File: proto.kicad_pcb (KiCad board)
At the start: 2 copper layers, 128 x 50.1 mm, 54 parts, among them IC1 WM8960CGEFL_V, J1 Micro_SD_Card, J10 CS, J11 BL, J12 BAT+, J13 BAT-, J14 L-, J15 L+, J16 R-, J17 R+, J2 AudioJack3, J3 USB_C_Receptacle_PowerOnly_6P, J4 GND, J5 VCC, J6 SCL, J7 SDA, J8 RES, J9 DC, SW1 SW_Push, SW2 SW_Push, SW3 SW_Push, SW4 SW_Push, SW5 SW_Push, SW6 SW_Push, SW7 SW_Push, SW8 SW_Push, U2 BQ24074RGT

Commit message: Fix PCB speaker markings
(R+ R- to L+ L-)
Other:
- board text added: "L+"
- board text added: "L-"

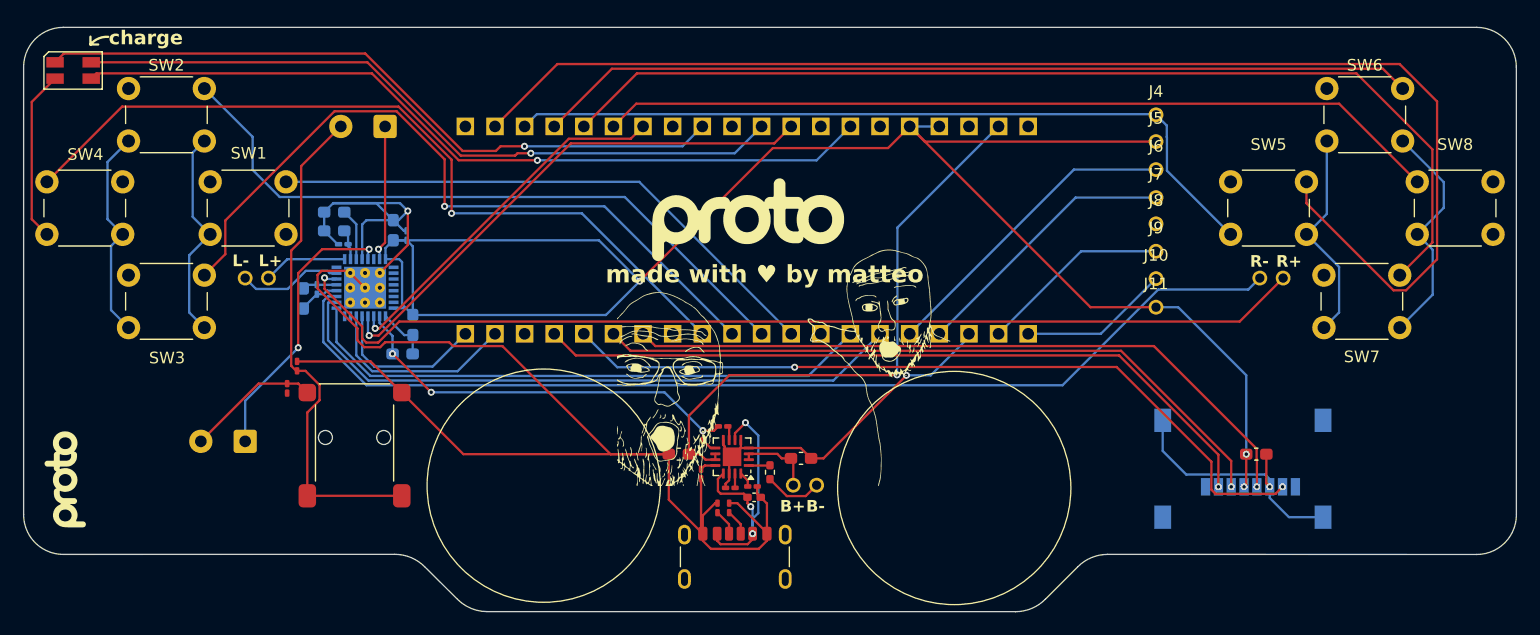
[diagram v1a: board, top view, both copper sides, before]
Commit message: Update hardware & software
Added a voltage divider to be able to measure battery level and added very basic firmware
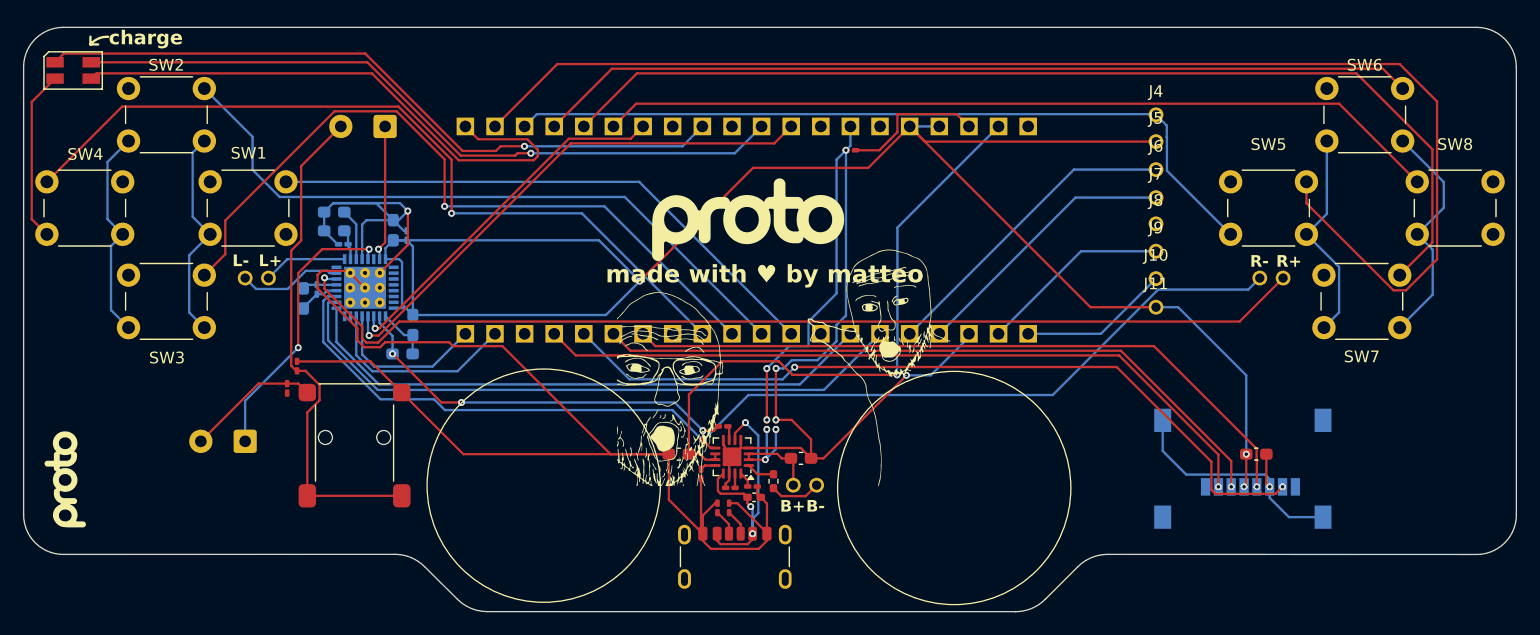
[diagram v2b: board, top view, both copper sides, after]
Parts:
- added C16: 100nF, Capacitor_SMD:C_0201_0603Metric_Pad0.64x0.40mm_HandSolder, F.Cu at (178.9, 96.0)
- added R10: 1M, Resistor_SMD:R_0201_0603Metric_Pad0.64x0.40mm_HandSolder, F.Cu at (172.5, 119.6)
- added R11: 1M, Resistor_SMD:R_0201_0603Metric_Pad0.64x0.40mm_HandSolder, F.Cu at (171.7, 119.6)
- moved TH1 0.83 mm to (172.3, 124.4)
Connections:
- C1 pad 2: GND -> BAT+
- C10 pad 1: GND -> BAT+
- C11 pad 1: GND -> BAT+
- C12 pad 1: GND -> BAT+
- C13 pad 1: GND -> BAT+
- C14 pad 1: GND -> BAT+
- C15 pad 1: GND -> BAT+
- C2 pad 2: GND -> BAT+
- C3 pad 2: GND -> BAT+
- C6 pad 2: GND -> BAT+
- C7 pad 2: GND -> BAT+
- C8 pad 2: GND -> BAT+
- C9 pad 2: GND -> BAT+
- D1 pad 4: GND -> BAT+
- IC1 pad 20: GND -> BAT+
- IC1 pad 24: GND -> BAT+
- IC1 pad 28: GND -> BAT+
- IC1 pad 33: GND -> BAT+
- IC1 pad 9: GND -> BAT+
- IC1 pad P$1: GND -> BAT+
- IC1 pad P$2: GND -> BAT+
- IC1 pad P$3: GND -> BAT+
- IC1 pad P$4: GND -> BAT+
- IC1 pad P$5: GND -> BAT+
- IC1 pad P$6: GND -> BAT+
- IC1 pad P$7: GND -> BAT+
- IC1 pad P$8: GND -> BAT+
- IC1 pad P$9: GND -> BAT+
- J1 pad 6: GND -> BAT+
- J1 pad SH: GND -> BAT+
- J2 pad S: GND -> BAT+
- J3 pad A12: GND -> BAT+
- J3 pad B12: GND -> BAT+
- J3 pad SH: GND -> BAT+
- J4 pad 1: GND -> BAT+
- R1 pad 1: GND -> BAT+
- R2 pad 1: GND -> BAT+
- R3 pad 2: GND -> BAT+
- R4 pad 2: GND -> BAT+
- R5 pad 2: GND -> BAT+
- R8 pad 1: GND -> BAT+
- R9 pad 1: GND -> BAT+
- SW1 pad 2: GND -> BAT+
- SW2 pad 2: GND -> BAT+
- SW3 pad 2: GND -> BAT+
- SW4 pad 2: GND -> BAT+
- SW5 pad 2: GND -> BAT+
- SW6 pad 2: GND -> BAT+
- SW7 pad 2: GND -> BAT+
- SW8 pad 2: GND -> BAT+
- U1 pad 3V3: +3.3V -> (no net)
- U1 pad GND: (no net) -> BAT+
- U1 pad GP0: CS -> (no net)
- U1 pad GP1: DC -> (no net)
- U1 pad GP22: B -> (no net)
- U1 pad GP26_A0: R -> (no net)
- U1 pad GP28_A2: G -> BAT+
- U2 pad 14: GND -> BAT+
- U2 pad 17: GND -> BAT+
- U2 pad 4: GND -> BAT+
- U2 pad 5: GND -> BAT+
- U2 pad 8: GND -> BAT+
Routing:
- net BAT+: track 6.66 -> 449.5 mm, vias 0 -> 11
- net GND: track 361.7 -> 0.00 mm, vias 3 -> 0
- net G: track 69.6 -> 49.3 mm, vias 1 -> 0
- net Net-(IC1-SPK_RN): track 90.4 -> 94.2 mm
- net VSYS: track 50.5 -> 52.5 mm
- net MISO: track 67.3 -> 68.1 mm
- net SDIN: track 54.4 -> 55.0 mm
- net BAT-: track 4.99 -> 4.37 mm
- net SCLK: track 49.7 -> 50.3 mm
- net TS: track 1.85 -> 2.43 mm

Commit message: UPDATED stuff again for software + hello world
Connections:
- U1 pad GP14: (no net) -> BLCK
- U1 pad GP27_A1: (no net) -> DACDAT
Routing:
- net DACDAT: track 17.1 -> 51.5 mm, vias 0 -> 1
- net BLCK: track 45.3 -> 14.9 mm, vias 1 -> 2
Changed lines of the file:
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@@
 			(layers "*.Cu" "*.Mask")
 			(remove_unused_layers no)
+			(net "BLCK")
 			(solder_mask_margin 0.102)
 		)
@@
 			(layers "*.Cu" "*.Mask")
 			(remove_unused_layers no)
+			(net "DACDAT")
 			(solder_mask_margin 0.102)
 		)
@@
 	)
 	(segment
-		(start 157.9325 110.1675)
-		(end 141.38 110.1675)
-		(width 0.2)
-		(layer "B.Cu")
-		(net "+3.3V")
-	)
-	(segment
 		(start 139.7025 103.76)
 		(end 157.33147 103.76)
@@
 	)
 	(segment
+		(start 158.574 109.526)
+		(end 142.0215 109.526)
+		(width 0.2)
+		(layer "B.Cu")
+		(net "+3.3V")
+	)
+	(segment
 		(start 207 109.5)
 		(end 205.1 109.5)
@@
 	)
 	(segment
-		(start 212.8375 115.3375)
-		(end 207 109.5)
+		(start 142.0215 109.526)
+		(end 141.38 110.1675)
 		(width 0.2)
 		(layer "B.Cu")
@@
 	)
 	(segment
-		(start 160.835735 107.264265)
-		(end 157.9325 110.1675)
+		(start 212.8375 115.3375)
+		(end 207 109.5)
 		(width 0.2)
 		(layer "B.Cu")
@@
 	)
 	(segment
+		(start 160.835735 107.264265)
+		(end 158.574 109.526)
+		(width 0.2)
+		(layer "B.Cu")
+		(net "+3.3V")
+	)
+	(segment
 		(start 157.33147 103.76)
 		(end 160.835735 107.264265)
@@
 	)
 	(segment
-		(start 154.920346 95.454)
-		(end 172.366 95.454)
+		(start 138.443849 111.930497)
+		(end 137.63 111.930497)
 		(width 0.2)
 		(layer "F.Cu")
@@
 	)
 	(segment
-		(start 172.366 95.454)
-		(end 173.82 94)
+		(start 140.248346 110.126)
+		(end 138.443849 111.930497)
 		(width 0.2)
 		(layer "F.Cu")
@@
 	)
 	(segment
-		(start 138.443849 111.930497)
-		(end 154.920346 95.454)
+		(start 148.42 110.126)
+		(end 140.248346 110.126)
 		(width 0.2)
 		(layer "F.Cu")
 		(net "BLCK")
 	)
-	(segment
-		(start 137.63 111.930497)
-		(end 138.443849 111.930497)
-		(width 0.2)
-		(layer "F.Cu")
+	(via
+		(at 148.42 110.126)
+		(size 0.6)
+		(drill 0.3)
+		(layers "F.Cu" "B.Cu")
 		(net "BLCK")
 	)
@@
 	)
 	(segment
+		(start 148.42 110.126)
+		(end 148.42 111.78)
+		(width 0.2)
+		(layer "B.Cu")
+		(net "BLCK")
+	)
+	(segment
 		(start 137.53 111.88)
 		(end 137.53 110.28)
@@
 	)
 	(segment
-		(start 137.897592 114.99)
-		(end 145.21 114.99)
+		(start 149.91 110.126)
+		(end 157.108 110.126)
+		(width 0.2)
+		(layer "F.Cu")
+		(net "DACDAT")
+	)
+	(segment
+		(start 173.234 94)
+		(end 173.82 94)
+		(width 0.2)
+		(layer "F.Cu")
+		(net "DACDAT")
+	)
+	(segment
+		(start 157.108 110.126)
+		(end 173.234 94)
+		(width 0.2)
+		(layer "F.Cu")
+		(net "DACDAT")
+	)
+	(via
+		(at 149.91 110.126)
+		(size 0.6)
+		(drill 0.3)
+		(layers "F.Cu" "B.Cu")
+		(net "DACDAT")
+	)
+	(segment
+		(start 149.91 110.126)
+		(end 149.91 110.722)
 		(width 0.2)
 		(layer "B.Cu")
@@
 	)
 	(segment
-		(start 145.21 114.99)
-		(end 148.42 111.78)
+		(start 149.906 110.726)
+		(end 149.906 112.834)
+		(width 0.2)
+		(layer "B.Cu")
+		(net "DACDAT")
+	)
+	(segment
+		(start 137.897593 114.99)
+		(end 136.53 113.622408)
+		(width 0.2)
+		(layer "B.Cu")
+		(net "DACDAT")
+	)
+	(segment
+		(start 149.91 110.722)
+		(end 149.906 110.726)
 		(width 0.2)
 		(layer "B.Cu")
@@
 	(segment
 		(start 136.53 113.622408)
-		(end 137.897592 114.99)
+		(end 136.53 110.28)
 		(width 0.2)
 		(layer "B.Cu")
@@
 	)
 	(segment
-		(start 136.53 110.28)
-		(end 136.53 113.622408)
+		(start 147.75 114.99)
+		(end 137.897593 114.99)
+		(width 0.2)
+		(layer "B.Cu")
+		(net "DACDAT")
+	)
+	(segment
+		(start 149.906 112.834)
+		(end 147.75 114.99)
 		(width 0.2)
 		(layer "B.Cu")
